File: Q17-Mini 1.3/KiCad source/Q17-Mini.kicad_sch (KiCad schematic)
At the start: 86 parts, among them J1 Input, J2-1 SPK+, J2-2 SPK-, J3-1 V+, J3-2 GND, J3-3 V-, Q1 IRF610, Q10 KSA992, Q11 ZVP2106A, Q12 BD139, Q13 IRF610, Q14 IRF9610, Q15 FQA46N15, Q16 FQA36P15, Q2 KSA992, Q3 KSC1845, Q4 IRF9610, Q5 FQP3P20, Q6 FQP3N30, Q7 KSC1845, Q8 ZVN4206AV, Q9 ZVP2106A, U1 OPA1641

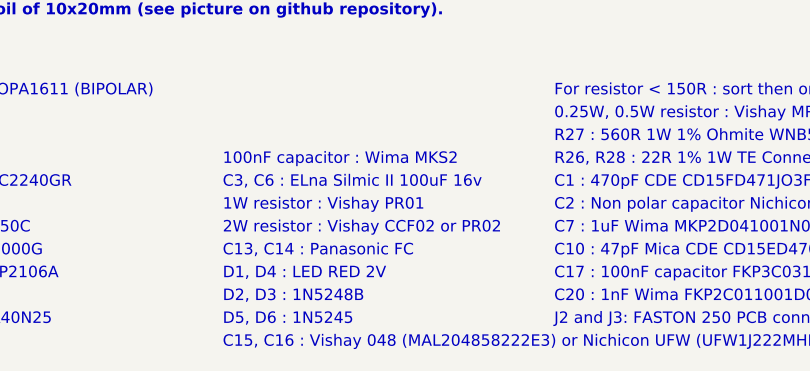
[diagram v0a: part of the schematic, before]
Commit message: Upgraded Q17-Mini 1.3
- New diagram.
- C13 and C14 now MAL215058221E3.
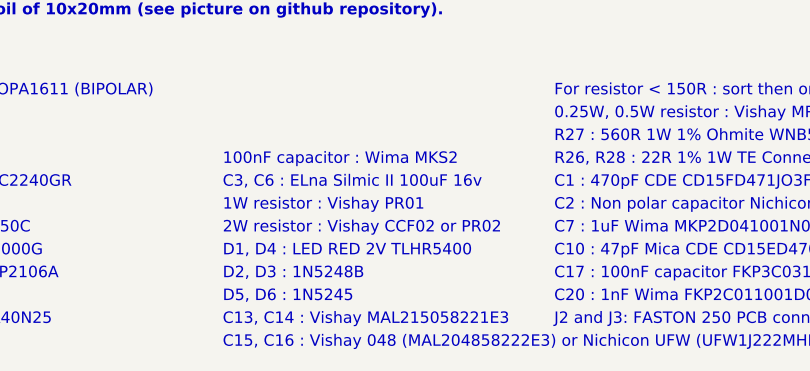
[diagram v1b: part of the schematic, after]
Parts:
- C13: Part# Panasonic FC EEU-FC1J221S -> Vishay MAL215058221E3
- C14: Part# Panasonic FC EEU-FC1J221S -> Vishat MAL215058221E3
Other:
- note added: "C13, C14 : Vishay MAL215058221E3"
- note added: "D1, D4 : LED RED 2V TLHR5400"
- note removed: "C13, C14 : Panasonic FC"
- note removed: "D1, D4 : LED RED 2V"
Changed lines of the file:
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@@
     (effects (font (size 1.27 1.27) (thickness 0.254) bold) (justify left bottom))
   )
-  (text "C13, C14 : Panasonic FC " (at 59.69 186.69 0)
+  (text "C13, C14 : Vishay MAL215058221E3" (at 59.69 194.31 0)
     (effects (font (size 1.27 1.27)) (justify left bottom))
   )
@@
     (effects (font (size 1.27 1.27)) (justify left bottom))
   )
-  (text "D2, D3 : 1N5248B" (at 59.69 191.77 0)
+  (text "D2, D3 : 1N5248B" (at 59.69 189.23 0)
     (effects (font (size 1.27 1.27)) (justify left bottom))
   )
@@
     (effects (font (size 1.27 1.27)) (justify left bottom))
   )
-  (text "D5, D6 : 1N5245" (at 59.69 194.31 0)
+  (text "D5, D6 : 1N5245" (at 59.69 191.77 0)
     (effects (font (size 1.27 1.27)) (justify left bottom))
   )
@@
     (effects (font (size 1.27 1.27)) (justify left bottom))
   )
-  (text "D1, D4 : LED RED 2V" (at 59.69 189.23 0)
+  (text "D1, D4 : LED RED 2V TLHR5400" (at 59.69 186.69 0)
     (effects (font (size 1.27 1.27)) (justify left bottom))
   )
@@
       (effects (font (size 1.27 1.27)) hide)
     )
-    (property "Part#" "Panasonic FC EEU-FC1J221S" (id 4) (at 205.74 40.64 0)
+    (property "Part#" "Vishay MAL215058221E3" (id 4) (at 205.74 40.64 0)
       (effects (font (size 1.27 1.27)) hide)
     )
@@
       (effects (font (size 1.27 1.27)) hide)
     )
-    (property "Part#" "Panasonic FC EEU-FC1J221S" (id 4) (at 205.74 125.73 0)
-      (effects (font (size 1.27 1.27)) hide)
-    )
+    (property "Part#" "Vishat MAL215058221E3" (id 4) (at 205.74 125.73 0)
+      (effects (font (size 1.27 1.27)) hide)
+    )

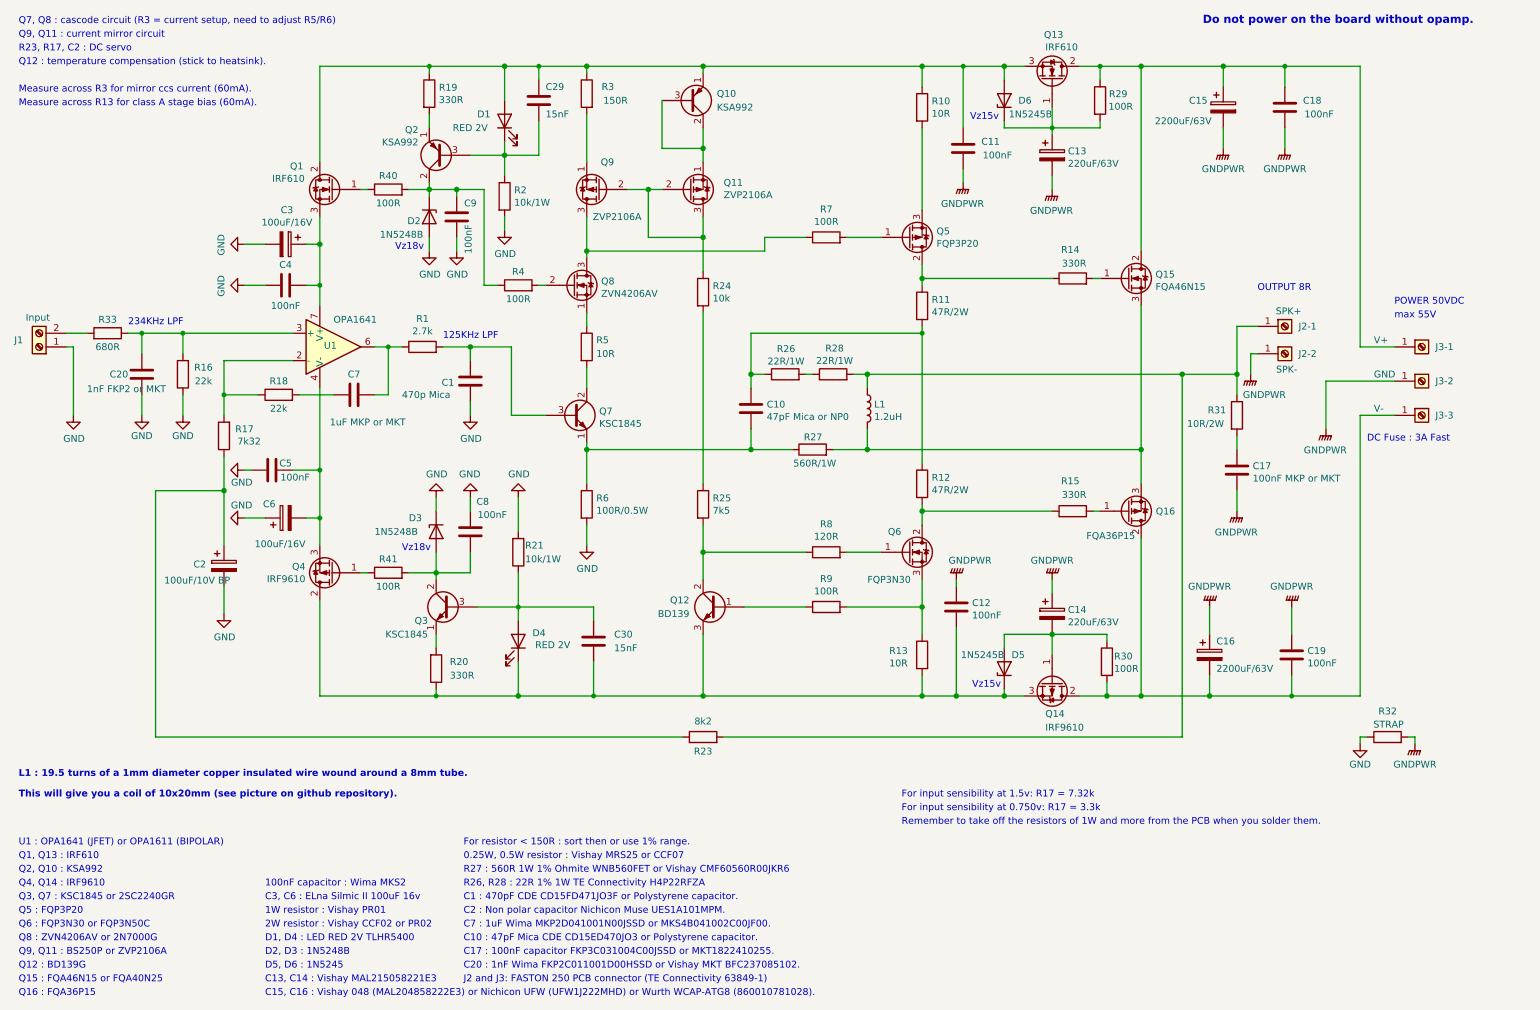
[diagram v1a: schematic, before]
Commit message: Update diagram for Q17-Mini 1.3
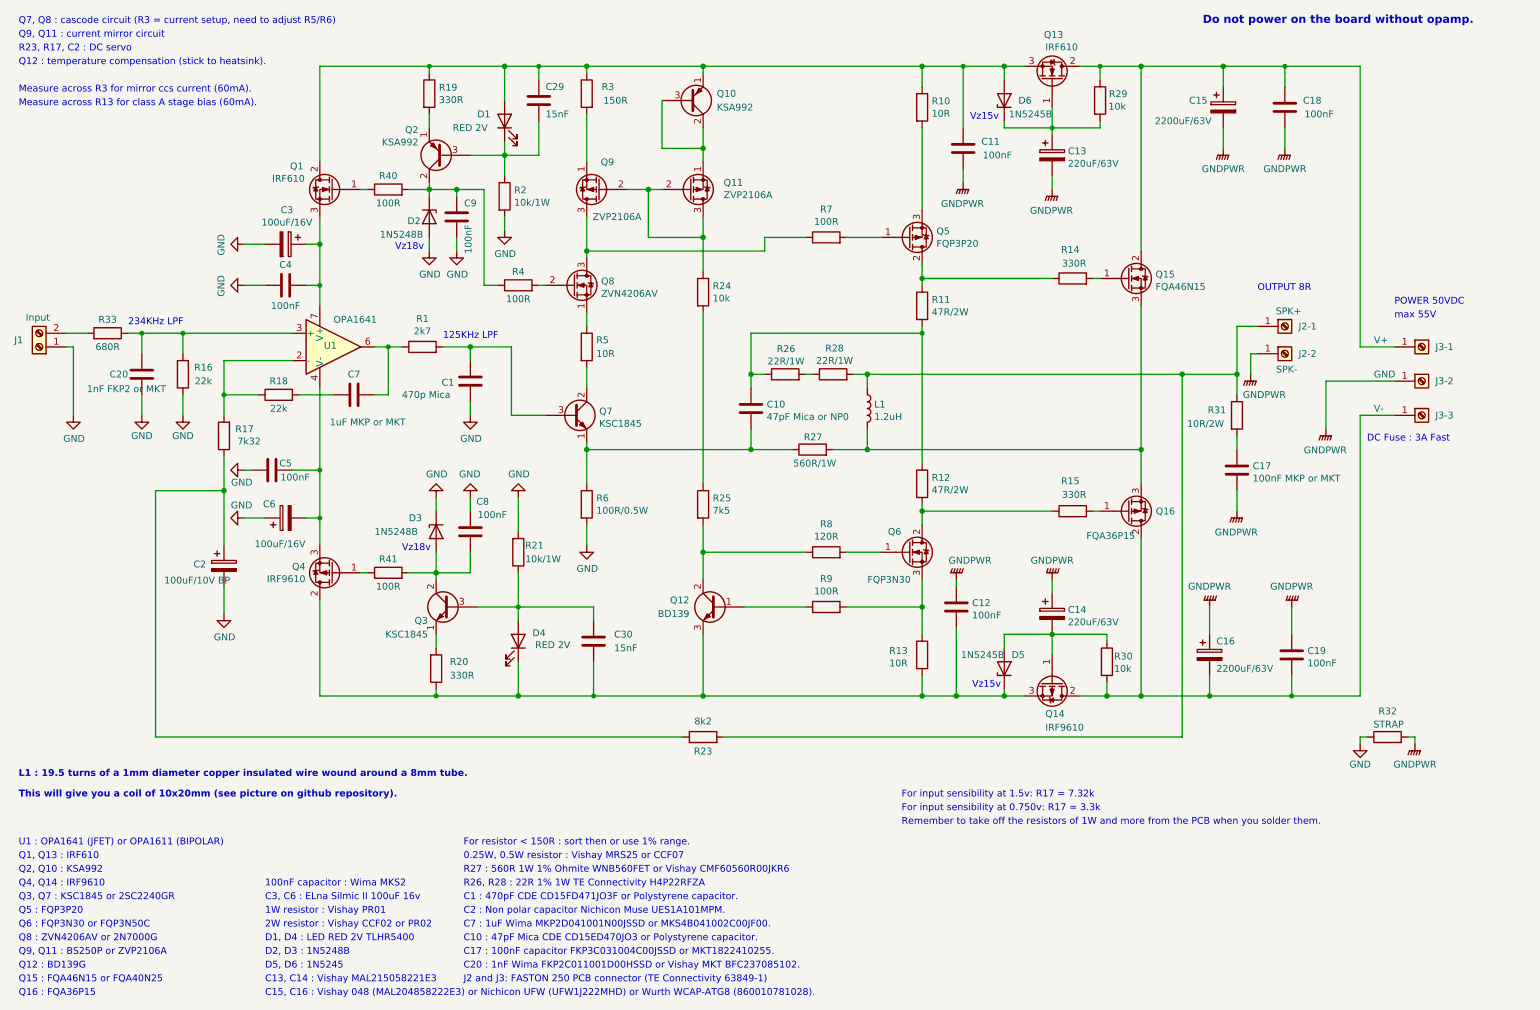
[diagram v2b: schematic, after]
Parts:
- R1: value 2.7k -> 2k7
- R29, R30: value 100R -> 10k; Part# MRS25000C1000FC100 -> MRS25000C1002FCT00
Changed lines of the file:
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@@
   (title_block
     (title "Q17-Mini Amplifier")
-    (date "2022-08-26")
+    (date "2022-08-29")
     (rev "1.3.8")
     (company "by eng. Tiberiu Vicol")
@@
     (in_bom yes) (on_board yes)
     (property "Reference" "R1" (id 0) (at 88.9 70.9738 90))
-    (property "Value" "2.7k" (id 1) (at 88.9 73.2725 90))
+    (property "Value" "2k7" (id 1) (at 88.9 73.2725 90))
     (property "Footprint" "Resistor_THT:R_Axial_DIN0207_L6.3mm_D2.5mm_P10.16mm_Horizontal" (id 2) (at 88.9 77.978 90)
       (effects (font (size 1.27 1.27)) hide)
@@
       (effects (font (size 1.27 1.27)) (justify left))
     )
-    (property "Value" "100R" (id 1) (at 216.2005 31.5986 0)
+    (property "Value" "10k" (id 1) (at 216.2005 31.5986 0)
       (effects (font (size 1.27 1.27)) (justify left))
     )
@@
       (effects (font (size 1.27 1.27)) hide)
     )
-    (property "Part#" "MRS25000C1000FC100" (id 4) (at 214.63 30.48 0)
+    (property "Part#" "MRS25000C1002FCT00" (id 4) (at 214.63 30.48 0)
       (effects (font (size 1.27 1.27)) hide)
     )
@@
       (effects (font (size 1.27 1.27)) (justify left))
     )
-    (property "Value" "100R" (id 1) (at 217.2359 135.9102 0)
+    (property "Value" "10k" (id 1) (at 217.2359 135.9102 0)
       (effects (font (size 1.27 1.27)) (justify left))
     )
@@
       (effects (font (size 1.27 1.27)) hide)
     )
-    (property "Part#" "MRS25000C1000FC100" (id 4) (at 215.9 134.62 0)
+    (property "Part#" "MRS25000C1002FCT00" (id 4) (at 215.9 134.62 0)
       (effects (font (size 1.27 1.27)) hide)
     )
@@
     )
     (path "/11ba1b60-15e3-49a9-9f8c-ecdcfb04f31a"
-      (reference "R1") (unit 1) (value "2.7k") (footprint "Resistor_THT:R_Axial_DIN0207_L6.3mm_D2.5mm_P10.16mm_Horizontal")
+      (reference "R1") (unit 1) (value "2k7") (footprint "Resistor_THT:R_Axial_DIN0207_L6.3mm_D2.5mm_P10.16mm_Horizontal")
     )
     (path "/66629faf-a191-4328-8001-bb82d5d2442f"
@@
     )
     (path "/6a502bca-5c03-4909-9915-ce87906e504a"
-      (reference "R29") (unit 1) (value "100R") (footprint "Resistor_THT:R_Axial_DIN0207_L6.3mm_D2.5mm_P10.16mm_Horizontal")
+      (reference "R29") (unit 1) (value "10k") (footprint "Resistor_THT:R_Axial_DIN0207_L6.3mm_D2.5mm_P10.16mm_Horizontal")
     )
     (path "/860cc2f6-176f-4935-b38a-f52437fa5513"
-      (reference "R30") (unit 1) (value "100R") (footprint "Resistor_THT:R_Axial_DIN0207_L6.3mm_D2.5mm_P10.16mm_Horizontal")
+      (reference "R30") (unit 1) (value "10k") (footprint "Resistor_THT:R_Axial_DIN0207_L6.3mm_D2.5mm_P10.16mm_Horizontal")
     )
     (path "/0b38258b-fc2c-4616-935a-ea7f37c299ab"

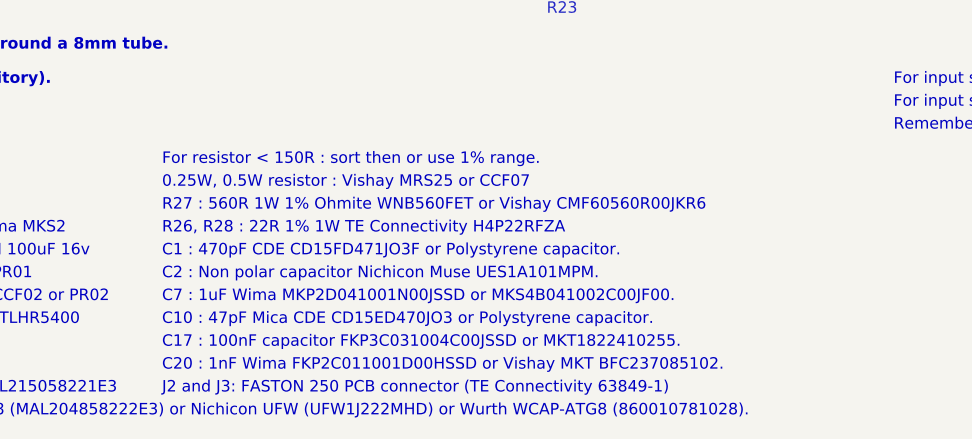
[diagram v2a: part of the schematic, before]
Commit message: Update diagram for Q17-Mini 1.3
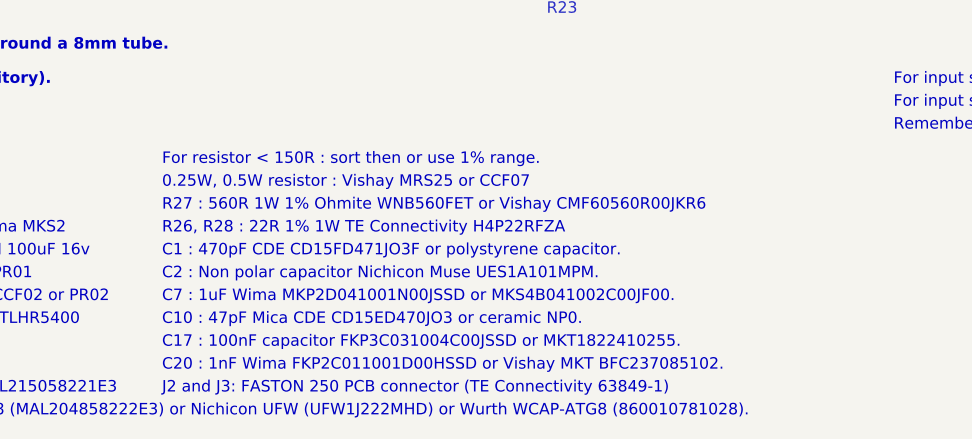
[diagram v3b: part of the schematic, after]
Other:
- note added: "C1 : 470pF CDE CD15FD471JO3F or polystyrene capacitor."
- note added: "C10 : 47pF Mica CDE CD15ED470JO3 or ceramic NP0."
- note removed: "C1 : 470pF CDE CD15FD471JO3F or Polystyrene capacitor."
- note removed: "C10 : 47pF Mica CDE CD15ED470JO3 or Polystyrene capacitor."
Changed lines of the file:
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@@
     (effects (font (size 1.27 1.27)) (justify left bottom))
   )
-  (text "C1 : 470pF CDE CD15FD471JO3F or Polystyrene capacitor."
+  (text "C1 : 470pF CDE CD15FD471JO3F or polystyrene capacitor."
     (at 96.52 179.07 0)
     (effects (font (size 1.27 1.27)) (justify left bottom))
@@
     (effects (font (size 1.27 1.27)) (justify left bottom))
   )
-  (text "C10 : 47pF Mica CDE CD15ED470JO3 or Polystyrene capacitor."
-    (at 96.52 186.69 0)
+  (text "C10 : 47pF Mica CDE CD15ED470JO3 or ceramic NP0." (at 96.52 186.69 0)
     (effects (font (size 1.27 1.27)) (justify left bottom))
   )

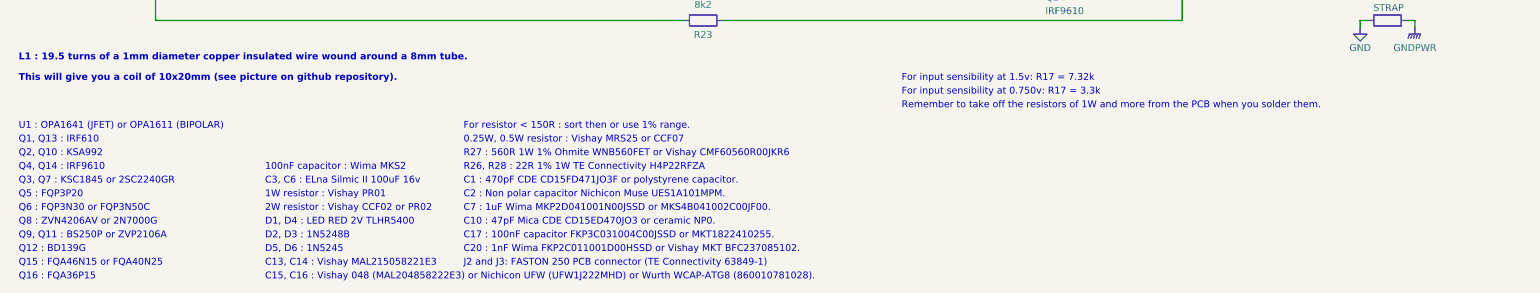
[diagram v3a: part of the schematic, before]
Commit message: Update diagram for Q17-Mini 1.3
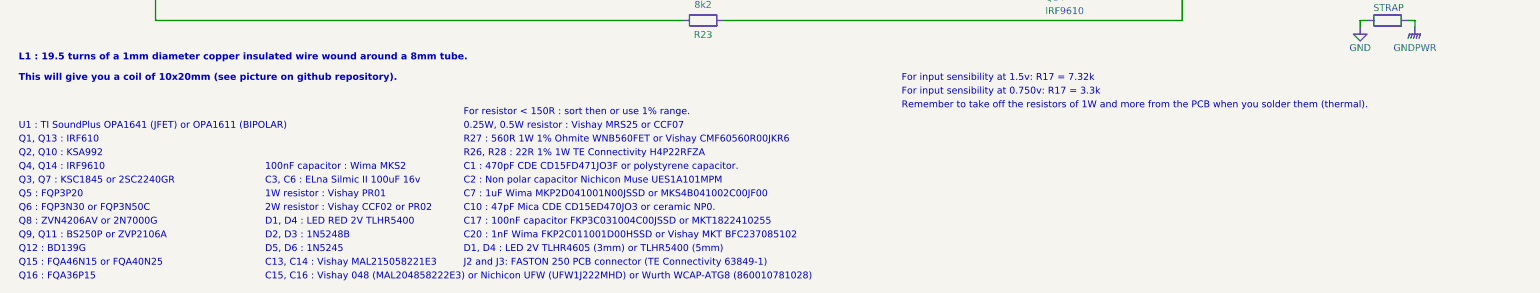
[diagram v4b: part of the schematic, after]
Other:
- note added: "C15, C16 : Vishay 048 (MAL204858222E3) or Nichicon UFW (UFW1J222MHD) or Wurth WCAP-ATG8 (860010781028)"
- note added: "C17 : 100nF capacitor FKP3C031004C00JSSD or MKT1822410255"
- note added: "C2 : Non polar capacitor Nichicon Muse UES1A101MPM"
- note added: "C20 : 1nF Wima FKP2C011001D00HSSD or Vishay MKT BFC237085102"
- note added: "C7 : 1uF Wima MKP2D041001N00JSSD or MKS4B041002C00JF00"
- note added: "D1, D4 : LED 2V TLHR4605 (3mm) or TLHR5400 (5mm)"
- note added: "Remember to take off the resistors of 1W and more from the PCB when you solder them (thermal)."
- note added: "U1 : TI SoundPlus OPA1641 (JFET) or OPA1611 (BIPOLAR)"
- note removed: "C15, C16 : Vishay 048 (MAL204858222E3) or Nichicon UFW (UFW1J222MHD) or Wurth WCAP-ATG8 (860010781028)."
- note removed: "C17 : 100nF capacitor FKP3C031004C00JSSD or MKT1822410255."
- note removed: "C2 : Non polar capacitor Nichicon Muse UES1A101MPM."
- note removed: "C20 : 1nF Wima FKP2C011001D00HSSD or Vishay MKT BFC237085102."
- note removed: "C7 : 1uF Wima MKP2D041001N00JSSD or MKS4B041002C00JF00."
- note removed: "Remember to take off the resistors of 1W and more from the PCB when you solder them."
- note removed: "U1 : OPA1641 (JFET) or OPA1611 (BIPOLAR)"
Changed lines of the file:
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@@
   (title_block
     (title "Q17-Mini Amplifier")
-    (date "2022-08-29")
+    (date "2022-08-31")
     (rev "1.3.8")
     (company "by eng. Tiberiu Vicol")
@@
     (stroke (width 0) (type solid) (color 0 0 0 0))
   )
-  (text "Remember to take off the resistors of 1W and more from the PCB when you solder them."
+  (text "Remember to take off the resistors of 1W and more from the PCB when you solder them (thermal)."
     (at 177.8 165.1 0)
     (effects (font (size 1.27 1.27)) (justify left bottom))
@@
     (effects (font (size 1.27 1.27)) (justify left bottom))
   )
-  (text "C2 : Non polar capacitor Nichicon Muse UES1A101MPM."
-    (at 96.52 181.61 0)
-    (effects (font (size 1.27 1.27)) (justify left bottom))
-  )
-  (text "U1 : OPA1641 (JFET) or OPA1611 (BIPOLAR)" (at 13.97 168.91 0)
-    (effects (font (size 1.27 1.27)) (justify left bottom))
-  )
-  (text "C15, C16 : Vishay 048 (MAL204858222E3) or Nichicon UFW (UFW1J222MHD) or Wurth WCAP-ATG8 (860010781028)."
+  (text "C2 : Non polar capacitor Nichicon Muse UES1A101MPM"
+    (at 96.52 179.07 0)
+    (effects (font (size 1.27 1.27)) (justify left bottom))
+  )
+  (text "U1 : TI SoundPlus OPA1641 (JFET) or OPA1611 (BIPOLAR)"
+    (at 13.97 168.91 0)
+    (effects (font (size 1.27 1.27)) (justify left bottom))
+  )
+  (text "C15, C16 : Vishay 048 (MAL204858222E3) or Nichicon UFW (UFW1J222MHD) or Wurth WCAP-ATG8 (860010781028)"
     (at 59.69 196.85 0)
     (effects (font (size 1.27 1.27)) (justify left bottom))
@@
   )
   (text "R27 : 560R 1W 1% Ohmite WNB560FET or Vishay CMF60560R00JKR6"
-    (at 96.52 173.99 0)
-    (effects (font (size 1.27 1.27)) (justify left bottom))
-  )
-  (text "0.25W, 0.5W resistor : Vishay MRS25 or CCF07" (at 96.52 171.45 0)
+    (at 96.52 171.45 0)
+    (effects (font (size 1.27 1.27)) (justify left bottom))
+  )
+  (text "D1, D4 : LED 2V TLHR4605 (3mm) or TLHR5400 (5mm)" (at 96.52 191.77 0)
+    (effects (font (size 1.27 1.27)) (justify left bottom))
+  )
+  (text "0.25W, 0.5W resistor : Vishay MRS25 or CCF07" (at 96.52 168.91 0)
     (effects (font (size 1.27 1.27)) (justify left bottom))
   )
@@
     (effects (font (size 1.27 1.27)) (justify left bottom))
   )
-  (text "C7 : 1uF Wima MKP2D041001N00JSSD or MKS4B041002C00JF00."
-    (at 96.52 184.15 0)
+  (text "C7 : 1uF Wima MKP2D041001N00JSSD or MKS4B041002C00JF00"
+    (at 96.52 181.61 0)
     (effects (font (size 1.27 1.27)) (justify left bottom))
   )
   (text "C1 : 470pF CDE CD15FD471JO3F or polystyrene capacitor."
-    (at 96.52 179.07 0)
+    (at 96.52 176.53 0)
     (effects (font (size 1.27 1.27)) (justify left bottom))
   )
@@
     (effects (font (size 1.27 1.27)) (justify left bottom))
   )
-  (text "R26, R28 : 22R 1% 1W TE Connectivity H4P22RFZA" (at 96.52 176.53 0)
+  (text "R26, R28 : 22R 1% 1W TE Connectivity H4P22RFZA" (at 96.52 173.99 0)
     (effects (font (size 1.27 1.27)) (justify left bottom))
   )
@@
     (effects (font (size 1.27 1.27)) (justify left bottom))
   )
-  (text "C10 : 47pF Mica CDE CD15ED470JO3 or ceramic NP0." (at 96.52 186.69 0)
+  (text "C10 : 47pF Mica CDE CD15ED470JO3 or ceramic NP0." (at 96.52 184.15 0)
     (effects (font (size 1.27 1.27)) (justify left bottom))
   )
@@
     (effects (font (size 1.27 1.27)) (justify left bottom))
   )
-  (text "For resistor < 150R : sort then or use 1% range." (at 96.52 168.91 0)
+  (text "For resistor < 150R : sort then or use 1% range." (at 96.52 166.37 0)
     (effects (font (size 1.27 1.27)) (justify left bottom))
   )
@@
     (effects (font (size 1.5 1.5) (thickness 0.254) bold) (justify left bottom))
   )
-  (text "C17 : 100nF capacitor FKP3C031004C00JSSD or MKT1822410255."
+  (text "C17 : 100nF capacitor FKP3C031004C00JSSD or MKT1822410255"
+    (at 96.52 186.69 0)
+    (effects (font (size 1.27 1.27)) (justify left bottom))
+  )
+  (text "C20 : 1nF Wima FKP2C011001D00HSSD or Vishay MKT BFC237085102"
     (at 96.52 189.23 0)
     (effects (font (size 1.27 1.27)) (justify left bottom))
   )
-  (text "C20 : 1nF Wima FKP2C011001D00HSSD or Vishay MKT BFC237085102."
-    (at 96.52 191.77 0)
-    (effects (font (size 1.27 1.27)) (justify left bottom))
-  )
